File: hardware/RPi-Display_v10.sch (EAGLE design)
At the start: 42 parts, among them IC1 ADS7846, Q1 N-CHN, SW1 SW4S, U1 TS5204-3V3, X1 PASSER, X2 PASSER, X3 PASSER, X4 PASSER

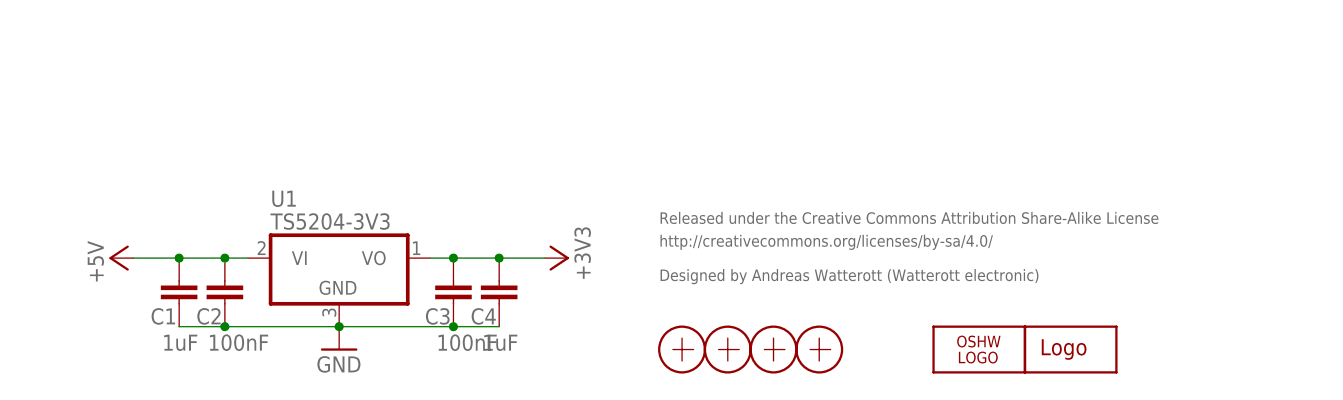
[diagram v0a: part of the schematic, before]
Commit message: updated schematics
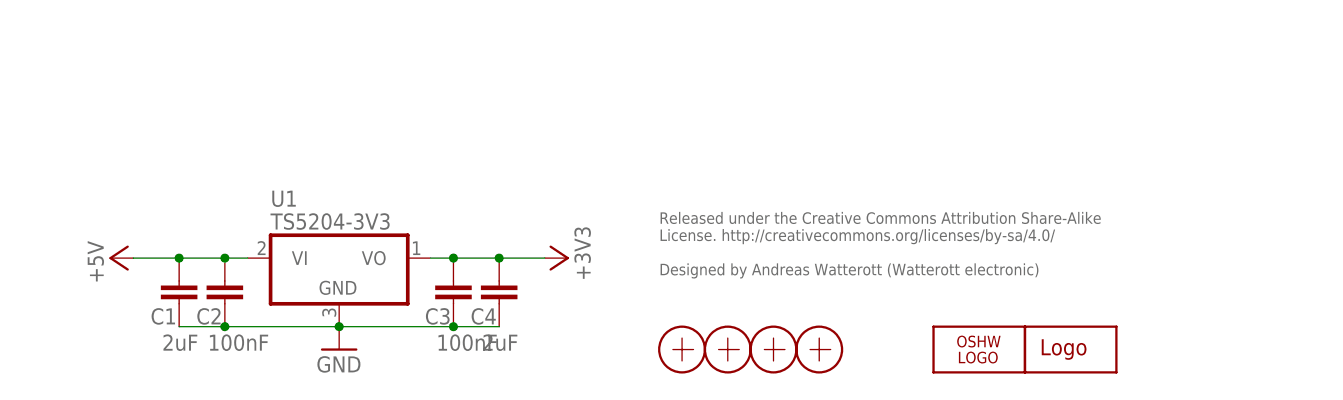
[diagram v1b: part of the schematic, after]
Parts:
- C1, C4: value 1uF -> 2uF
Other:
- note added: "Released under the Creative Commons Attribution Share-Alike License. http://creativecommons.org/licenses/by-sa/4.0/ Designed by Andreas Watterott (Watterott electronic)"
- note removed: "Designed by Andreas Watterott (Watterott electronic)"
- note removed: "Released under the Creative Commons Attribution Share-Alike License"
- note removed: "http://creativecommons.org/licenses/by-sa/4.0/"
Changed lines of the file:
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@@
 <?xml version="1.0" encoding="utf-8"?>
 <!DOCTYPE eagle SYSTEM "eagle.dtd">
-<eagle version="6.6.0">
+<eagle version="7.5.0">
 <drawing>
 <settings>
@@
 <layer number="51" name="tDocu" color="7" fill="1" visible="no" active="no"/>
 <layer number="52" name="bDocu" color="7" fill="1" visible="no" active="no"/>
-<layer number="53" name="tCopper" color="7" fill="11" visible="no" active="no"/>
-<layer number="54" name="bCopper" color="7" fill="1" visible="no" active="no"/>
-<layer number="56" name="wert" color="7" fill="1" visible="no" active="no"/>
 <layer number="91" name="Nets" color="2" fill="1" visible="yes" active="yes"/>
 <layer number="92" name="Busses" color="1" fill="1" visible="yes" active="yes"/>
@@
 <layer number="97" name="Info" color="7" fill="1" visible="yes" active="yes"/>
 <layer number="98" name="Guide" color="6" fill="1" visible="yes" active="yes"/>
-<layer number="100" name="Muster" color="7" fill="1" visible="no" active="no"/>
-<layer number="217" name="217bmp" color="18" fill="1" visible="no" active="no"/>
-<layer number="218" name="218bmp" color="19" fill="1" visible="no" active="no"/>
-<layer number="219" name="219bmp" color="20" fill="1" visible="no" active="no"/>
-<layer number="220" name="220bmp" color="21" fill="1" visible="no" active="no"/>
-<layer number="221" name="221bmp" color="22" fill="1" visible="no" active="no"/>
-<layer number="222" name="222bmp" color="23" fill="1" visible="no" active="no"/>
-<layer number="223" name="223bmp" color="24" fill="1" visible="no" active="no"/>
-<layer number="224" name="224bmp" color="25" fill="1" visible="no" active="no"/>
 <layer number="250" name="Descript" color="3" fill="1" visible="yes" active="yes"/>
-<layer number="251" name="SMDround" color="12" fill="11" visible="no" active="no"/>
 </layers>
 <schematic xreflabel="%F%N/%S.%C%R" xrefpart="/%S.%C%R">
@@
 <part name="C3" library="rcl" deviceset="C-EU" device="C0603" value="100nF"/>
 <part name="U1" library="Voltage-Reg" deviceset="TS5204" device="" value="TS5204-3V3"/>
-<part name="C1" library="rcl" deviceset="C-EU" device="C0603" value="1uF"/>
+<part name="C1" library="rcl" deviceset="C-EU" device="C0603" value="2uF"/>
 <part name="X1" library="SMD" deviceset="PASSER" device=""/>
 <part name="X2" library="SMD" deviceset="PASSER" device=""/>
@@
 <part name="R7" library="rcl" deviceset="R-EU_" device="R0603" value="10k"/>
 <part name="+3V6" library="supply1" deviceset="+3V3" device=""/>
-<part name="C4" library="rcl" deviceset="C-EU" device="C0603" value="1uF"/>
+<part name="C4" library="rcl" deviceset="C-EU" device="C0603" value="2uF"/>
 <part name="C8" library="rcl" deviceset="C-EU" device="C0603" value="100nF"/>
 <part name="C6" library="rcl" deviceset="C-EU" device="C0603" value="100nF"/>
@@
 <text x="36.83" y="162.56" size="3.81" layer="250">2.8" Display with Touchpanel</text>
 <text x="180.34" y="162.56" size="3.81" layer="250">Raspberry Pi</text>
-<text x="162.56" y="21.59" size="1.27" layer="95">Released under the Creative Commons Attribution Share-Alike License</text>
-<text x="162.56" y="19.05" size="1.27" layer="95">http://creativecommons.org/licenses/by-sa/4.0/</text>
-<text x="162.56" y="15.24" size="1.27" layer="95">Designed by Andreas Watterott (Watterott electronic)</text>
+<text x="162.56" y="22.86" size="1.27" layer="95" align="top-left">Released under the Creative Commons Attribution Share-Alike
+License. http://creativecommons.org/licenses/by-sa/4.0/
+Designed by Andreas Watterott (Watterott electronic)</text>
 <text x="128.27" y="100.33" size="3.81" layer="250">Touch Controller</text>
 <text x="139.7" y="59.69" size="1.778" layer="95">or TSC2046</text>
